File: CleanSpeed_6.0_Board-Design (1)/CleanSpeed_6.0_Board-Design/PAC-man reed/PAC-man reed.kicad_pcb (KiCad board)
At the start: 2 copper layers, 75.5 x 74.2 mm, 43 parts, among them IC1 LTC6820HMS#3ZZPBF, IC2 LTC6820HMS#3ZZPBF, J1 Conn_01x01, J2 Conn_01x01, J3 Conn_01x01, J4 Conn_01x14, J5 Conn_01x02, J6 JST PH, J7 Conn_01x02, J8 Conn_01x02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

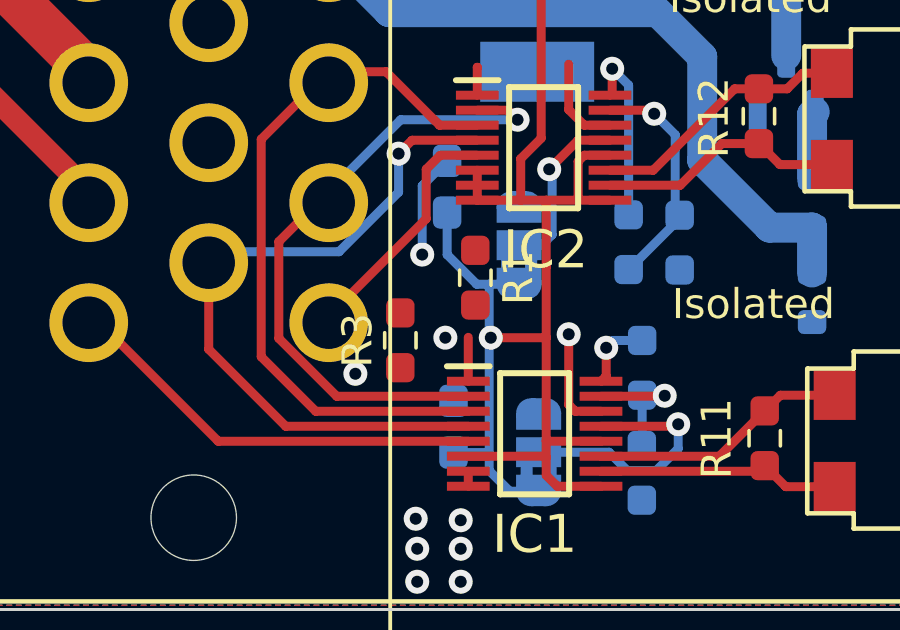
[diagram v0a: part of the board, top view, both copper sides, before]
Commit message: Pre-charge routing
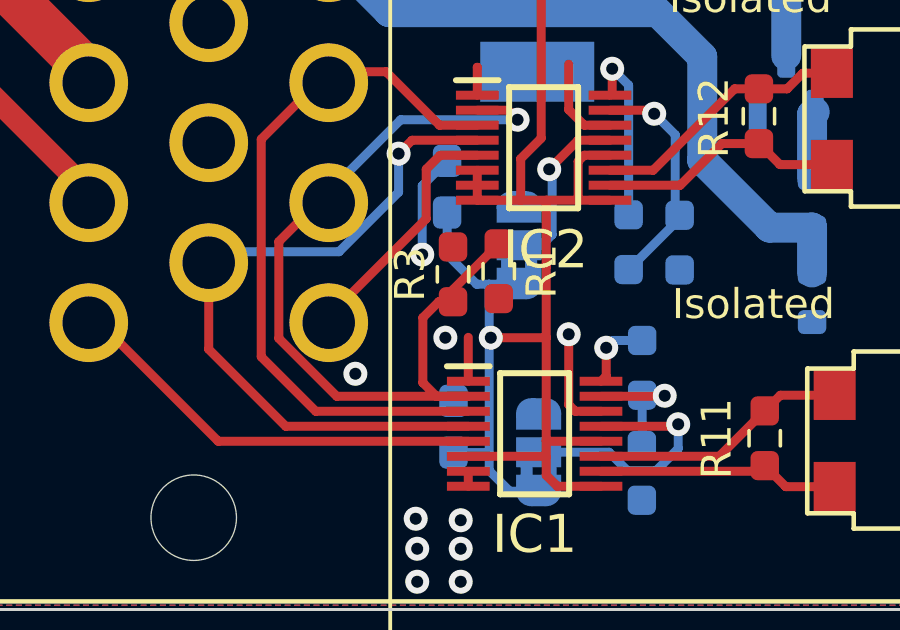
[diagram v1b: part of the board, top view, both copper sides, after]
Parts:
- moved R3 2.81 mm to (143.3, 119.9)
- moved R1 0.81 mm to (144.8, 119.8)
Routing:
- net /MOSI: track 21.5 -> 29.1 mm
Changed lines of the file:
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@@
 	(footprint "Resistor_SMD:R_0603_1608Metric_Pad0.98x0.95mm_HandSolder"
 		(layer "F.Cu")
-		(at 141.5 122.0875 90)
+		(at 143.256 119.888 90)
 		(descr "Resistor SMD 0603 (1608 Metric), square (rectangular) end terminal, IPC_7351 nominal with elongated pad for handsoldering. (Body size source: IPC-SM-782 page 72, https://www.pcb-3d.com/wordpress/wp-content/uploads/ipc-sm-782a_amendment_1_and_2.pdf), generated with kicad-footprint-generator")
 		(tags "resistor handsolder")
@@
 	(footprint "Resistor_SMD:R_0603_1608Metric_Pad0.98x0.95mm_HandSolder"
 		(layer "F.Cu")
-		(at 144 120 -90)
+		(at 144.78 119.7845 -90)
 		(descr "Resistor SMD 0603 (1608 Metric), square (rectangular) end terminal, IPC_7351 nominal with elongated pad for handsoldering. (Body size source: IPC-SM-782 page 72, https://www.pcb-3d.com/wordpress/wp-content/uploads/ipc-sm-782a_amendment_1_and_2.pdf), generated with kicad-footprint-generator")
 		(tags "resistor handsolder")
@@
 	)
 	(segment
+		(start 142.781 120.8005)
+		(end 143.256 120.8005)
+		(width 0.3)
+		(layer "F.Cu")
+		(net 9)
+	)
+	(segment
+		(start 143.764498 123.952399)
+		(end 142.701998 123.952399)
+		(width 0.3)
+		(layer "F.Cu")
+		(net 9)
+	)
+	(segment
+		(start 142.25 123.500401)
+		(end 142.25 121.3315)
+		(width 0.3)
+		(layer "F.Cu")
+		(net 9)
+	)
+	(segment
 		(start 143.764498 123.952399)
 		(end 139.379397 123.952399)
@@
 	)
 	(segment
+		(start 142.701998 123.952399)
+		(end 142.25 123.500401)
+		(width 0.3)
+		(layer "F.Cu")
+		(net 9)
+	)
+	(segment
 		(start 137.449497 122.022499)
 		(end 137.449497 118.797499)
@@
 	)
 	(segment
+		(start 143.256 120.396)
+		(end 144.78 118.872)
+		(width 0.3)
+		(layer "F.Cu")
+		(net 9)
+	)
+	(segment
+		(start 143.256 120.8005)
+		(end 143.256 120.396)
+		(width 0.3)
+		(layer "F.Cu")
+		(net 9)
+	)
+	(segment
 		(start 144.064498 114.417499)
 		(end 145.09002 114.417499)
@@
 		(width 0.3)
 		(layer "F.Cu")
+		(net 9)
+	)
+	(segment
+		(start 142.25 121.3315)
+		(end 142.781 120.8005)
+		(width 0.3)
+		(layer "F.Cu")
